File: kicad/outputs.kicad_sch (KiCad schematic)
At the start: 50 parts, among them J4 OUT Q1, J5 OUT Q2, J6 OUT Q3, J7 OUT Q4, J8 OUT Q5, J9 OUT Q6, Q1 AOD4184A, Q2 AOD4184A, Q3 AOD4184A, Q4 AOD4184A, Q5 AOD4184A, Q6 AOD4184A, U3 74HCT244D

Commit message: kicad: push-in spring terminals (Kangnex WJ250B), 8 A total
All 18 screw terminals replaced by Ningbo Kangnex WJ250B push-in spring
terminals (LCSC C8454 2-pole, C8420 3-pole; 3.5 mm pitch, staggered
pins, 8 A IEC). New footprints from the EasyEDA pad data and the maker
drawing (wire entry on the pin-1 side, facing the board edge) and
simple 3D models. Board total current reduced to 8 A: fuse 8 A
(Littelfuse 0154008.DR, LCSC C206919). Board: footprints swapped with
nets and schematic links kept, edges re-placed for the deeper bodies.
ERC 0; DRC unchanged (known J2/Zero-hole overlap, silk, unrouted).
Docs: BOM/README (8 A budget, 5.3 mm input path, cost ~35 EUR/board).

Co-Authored-By: Claude Opus 5.5 <noreply@anthropic.com>
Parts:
- J4, J5, J6, J7, J8, J9: footprint TerminalBlock_Phoenix:TerminalBlock_Phoenix_MKDS-1,5-2-5.08_1x02_P5.08mm_Horizontal -> aquaPCB:TerminalBlock_Kangnex_WJ250B-3.5-02P_P3.50mm_Staggered; LCSC (none) -> C8454; Reichelt AKL 101-02 -> (none)
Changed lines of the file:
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@@
 			)
 		)
-		(property "Footprint" "TerminalBlock_Phoenix:TerminalBlock_Phoenix_MKDS-1,5-2-5.08_1x02_P5.08mm_Horizontal"
+		(property "Footprint" "aquaPCB:TerminalBlock_Kangnex_WJ250B-3.5-02P_P3.50mm_Staggered"
 			(at 254 247.65 0)
 			(hide yes)
@@
 			)
 		)
-		(property "Reichelt" "AKL 101-02"
+		(property "LCSC" "C8454"
 			(at 254 247.65 0)
 			(hide yes)
@@
 			)
 		)
-		(property "Footprint" "TerminalBlock_Phoenix:TerminalBlock_Phoenix_MKDS-1,5-2-5.08_1x02_P5.08mm_Horizontal"
+		(property "Footprint" "aquaPCB:TerminalBlock_Kangnex_WJ250B-3.5-02P_P3.50mm_Staggered"
 			(at 254 223.52 0)
 			(hide yes)
@@
 			)
 		)
-		(property "Reichelt" "AKL 101-02"
+		(property "LCSC" "C8454"
 			(at 254 223.52 0)
 			(hide yes)
@@
 			)
 		)
-		(property "Footprint" "TerminalBlock_Phoenix:TerminalBlock_Phoenix_MKDS-1,5-2-5.08_1x02_P5.08mm_Horizontal"
+		(property "Footprint" "aquaPCB:TerminalBlock_Kangnex_WJ250B-3.5-02P_P3.50mm_Staggered"
 			(at 254 175.26 0)
 			(hide yes)
@@
 			)
 		)
-		(property "Reichelt" "AKL 101-02"
+		(property "LCSC" "C8454"
 			(at 254 175.26 0)
 			(hide yes)
@@
 			)
 		)
-		(property "Footprint" "TerminalBlock_Phoenix:TerminalBlock_Phoenix_MKDS-1,5-2-5.08_1x02_P5.08mm_Horizontal"
+		(property "Footprint" "aquaPCB:TerminalBlock_Kangnex_WJ250B-3.5-02P_P3.50mm_Staggered"
 			(at 254 151.13 0)
 			(hide yes)
@@
 			)
 		)
-		(property "Reichelt" "AKL 101-02"
+		(property "LCSC" "C8454"
 			(at 254 151.13 0)
 			(hide yes)
@@
 			)
 		)
-		(property "Footprint" "TerminalBlock_Phoenix:TerminalBlock_Phoenix_MKDS-1,5-2-5.08_1x02_P5.08mm_Horizontal"
+		(property "Footprint" "aquaPCB:TerminalBlock_Kangnex_WJ250B-3.5-02P_P3.50mm_Staggered"
 			(at 254 127 0)
 			(hide yes)
@@
 			)
 		)
-		(property "Reichelt" "AKL 101-02"
+		(property "LCSC" "C8454"
 			(at 254 127 0)
 			(hide yes)
@@
 			)
 		)
-		(property "Footprint" "TerminalBlock_Phoenix:TerminalBlock_Phoenix_MKDS-1,5-2-5.08_1x02_P5.08mm_Horizontal"
+		(property "Footprint" "aquaPCB:TerminalBlock_Kangnex_WJ250B-3.5-02P_P3.50mm_Staggered"
 			(at 254 199.39 0)
 			(hide yes)
@@
 			)
 		)
-		(property "Reichelt" "AKL 101-02"
+		(property "LCSC" "C8454"
 			(at 254 199.39 0)
 			(hide yes)

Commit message: kicad: routing progress (by hand)
Co-Authored-By: Claude Opus 5.5 (1M context) <noreply@anthropic.com>
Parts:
- D11: value LED green -> GPIO12
- D13: value LED green -> GPIO13
- D15: value LED green -> GPIO16
- D17: value LED green -> GPIO26
- D7: value LED green -> GPIO18
- D9: value LED green -> GPIO19
- J4: value OUT Q1 -> OUT G18
- J5: value OUT Q2 -> OUT G19
- J6: value OUT Q3 -> OUT G12
- J7: value OUT Q4 -> OUT G13
- J8: value OUT Q5 -> OUT G16
- J9: value OUT Q6 -> OUT G26
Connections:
- net Q1_G: no longer names the net of Q1.1 (G), R14.2, R15.1
- net Q1_LED: no longer names the net of D7.2 (A), R16.2
- net Q1_OUT: no longer names the net of D6.2 (A), J4.2 (Pin_2), Q1.2 (D)
- net Q2_G: no longer names the net of Q2.1 (G), R17.2, R18.1
- net Q2_LED: no longer names the net of D9.2 (A), R19.2
- net Q2_OUT: no longer names the net of D8.2 (A), J5.2 (Pin_2), Q2.2 (D)
- net Q3_G: no longer names the net of Q3.1 (G), R20.2, R21.1
- net Q3_LED: no longer names the net of D11.2 (A), R22.2
- net Q3_OUT: no longer names the net of D10.2 (A), J6.2 (Pin_2), Q3.2 (D)
- net Q4_G: no longer names the net of Q4.1 (G), R23.2, R24.1
- net Q4_LED: no longer names the net of D13.2 (A), R25.2
- net Q4_OUT: no longer names the net of D12.2 (A), J7.2 (Pin_2), Q4.2 (D)
- net Q5_G: no longer names the net of Q5.1 (G), R26.2, R27.1
- net Q5_LED: no longer names the net of D15.2 (A), R28.2
- net Q5_OUT: no longer names the net of D14.2 (A), J8.2 (Pin_2), Q5.2 (D)
- net Q6_G: no longer names the net of Q6.1 (G), R29.2, R30.1
- net Q6_LED: no longer names the net of D17.2 (A), R31.2
- net Q6_OUT: no longer names the net of D16.2 (A), J9.2 (Pin_2), Q6.2 (D)
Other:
- moved on the sheet: D10, D11, D12, D13, D14, D15, D16, D17, D6, D7, D8, D9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

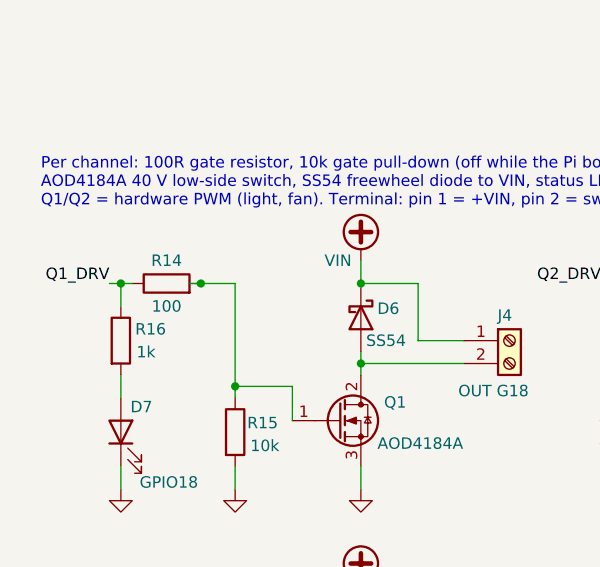
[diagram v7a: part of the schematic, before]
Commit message: kicad: drop J10, fix S1 output shorted to SSR_V
- J10 (ULN2803 spare header) removed from schematic and board; the four
  unused ULN channels (U4 pins 5-8, 11-14) are marked no-connect
- schematic: a wire in front of J11 joined its two stubs, shorting the
  S1 output (U4 O1, D18, J11 pin 2) to SSR_V; removed. The board carried
  the merged net too but no copper joined both sides; pads and tracks
  are split again (SSR side now Net-(J11-Pin_1), S1 side Net-(D18-K))
- dangling 1.27 mm wire at R14 (outputs sheet) removed
ERC 0; DRC with schematic parity: only the known J2/Zero-hole overlap
and unrouted nets. Docs: J10 removed from README/BOM.

Co-Authored-By: Claude Opus 5.5 (1M context) <noreply@anthropic.com>
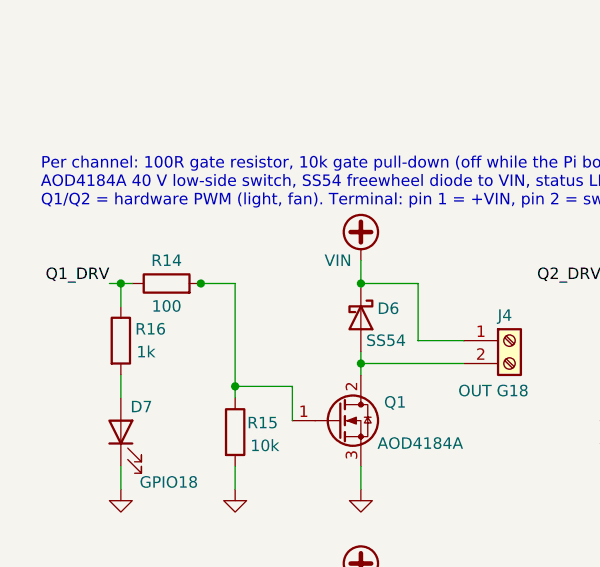
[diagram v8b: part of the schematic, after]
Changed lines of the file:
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@@
-	(wire
-		(pts
-			(xy 41.91 123.19) (xy 43.18 123.19)
-		)
-		(stroke
-			(width 0)
-			(type default)
-		)
-	)
 	(wire
 		(pts
